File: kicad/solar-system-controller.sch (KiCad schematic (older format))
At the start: 18 parts, among them J1 Raspberry_Pi_2_3, J2 Line_In, U1 MCP3008, U2 500 Gain, U3 1000 Gain

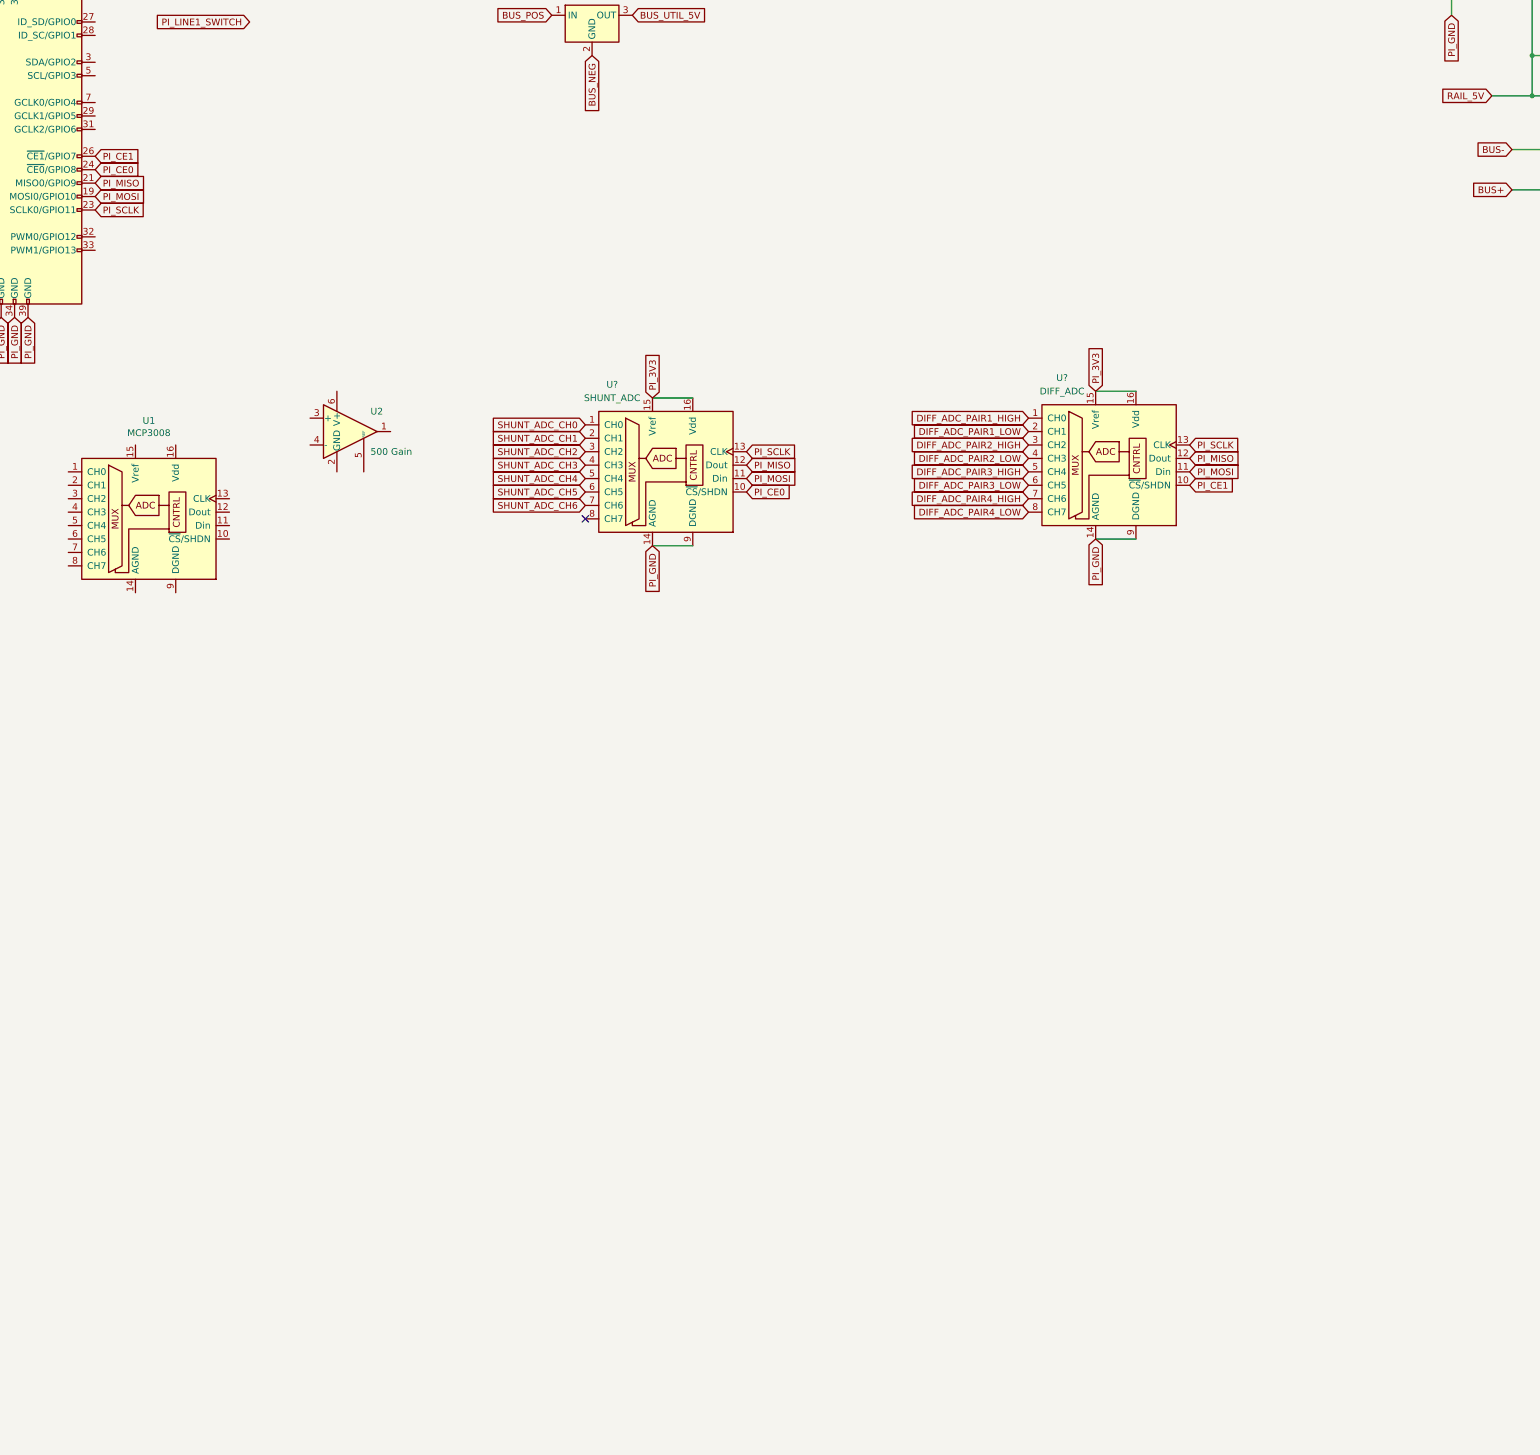
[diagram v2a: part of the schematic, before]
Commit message: Added a mux for the ADCs.
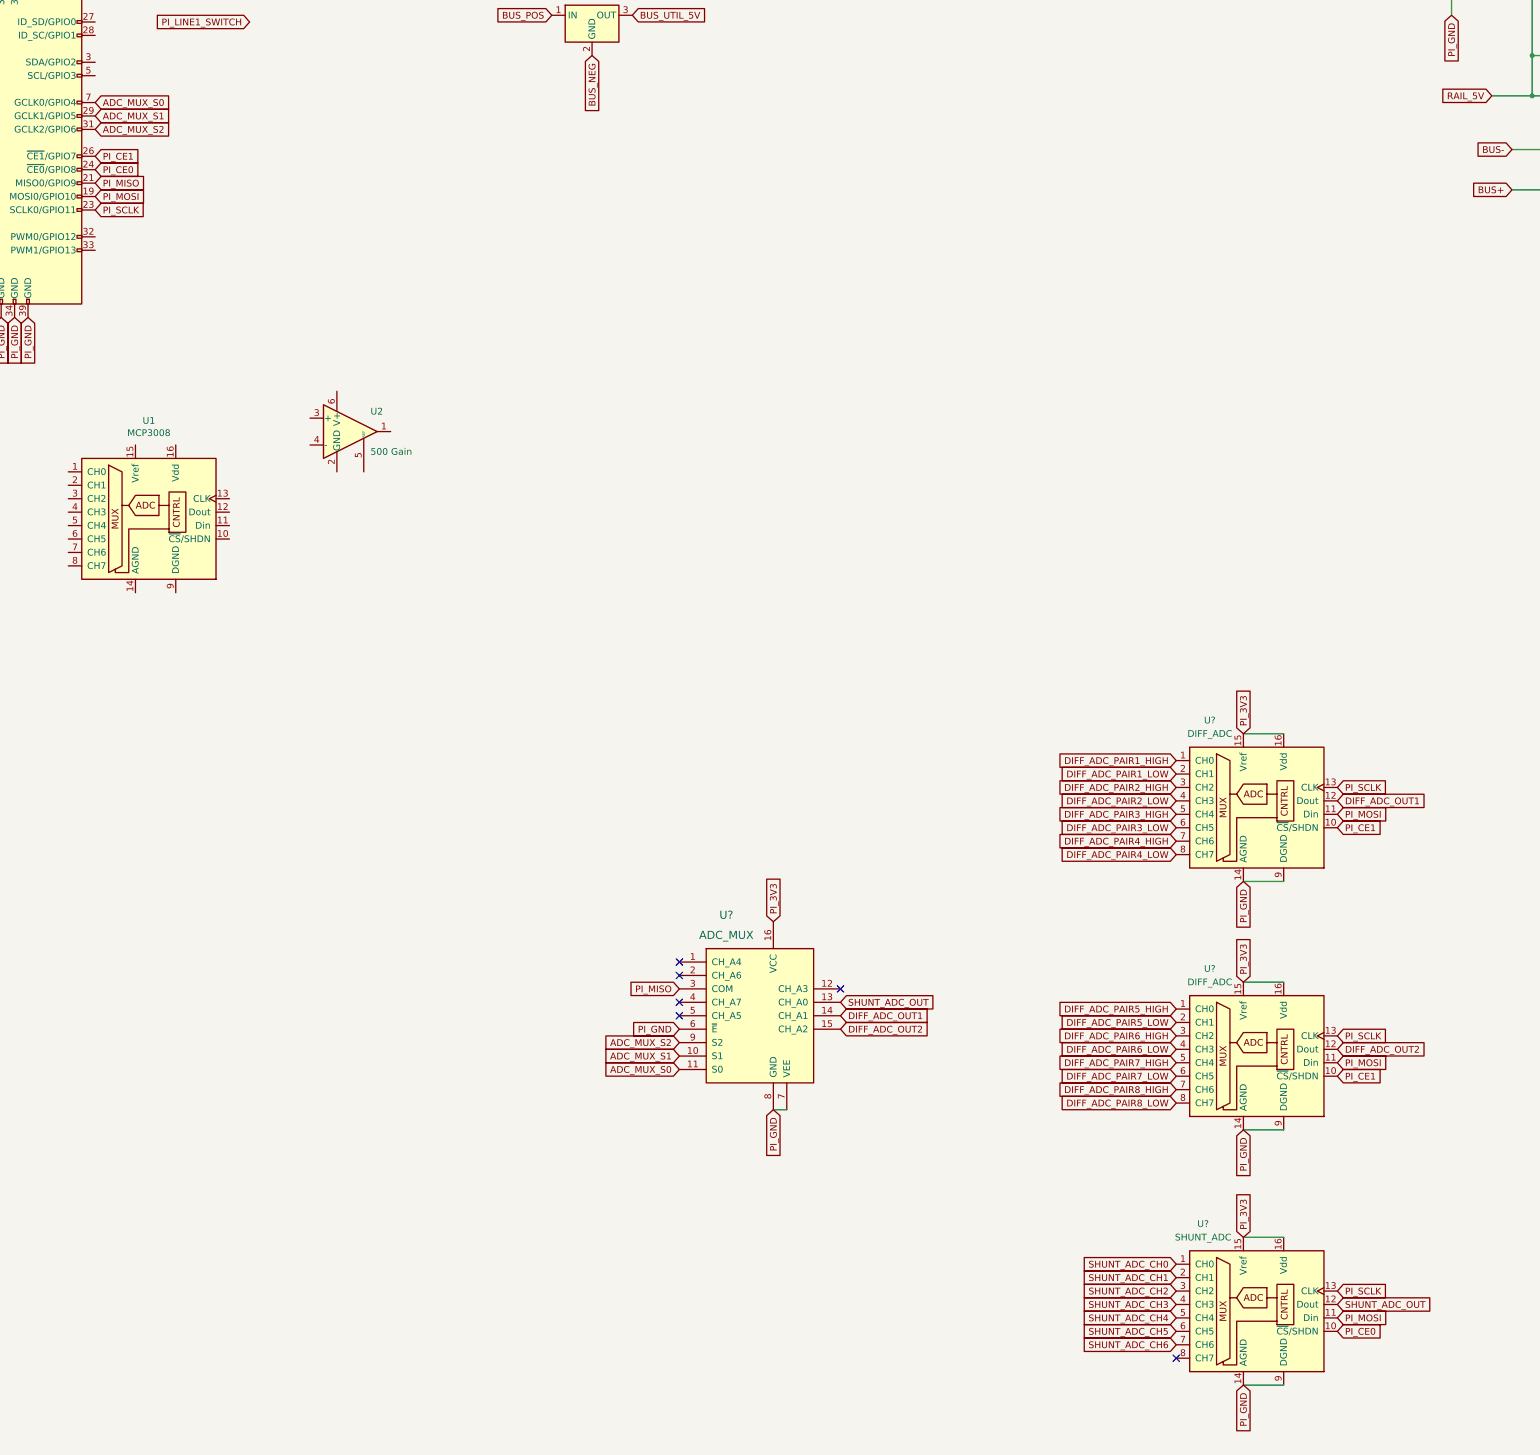
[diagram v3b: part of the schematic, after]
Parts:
- added U?: DIFF_ADC, Package_DIP:DIP-16_W7.62mm, symbol Analog_ADC:MCP3008
- added U?: ADC_MUX, digikey-footprints:DIP-16_W7.62mm, symbol dk_Interface-Analog-Switches-Multiplexers-Demultiplexers:CD74HC4051E
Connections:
- net DIFF_ADC_PAIR1_HIGH: now also U?.1 (CH0); no longer U?.1 (CH0)
- net DIFF_ADC_PAIR1_LOW: now also U?.2 (CH1); no longer U?.2 (CH1)
- net DIFF_ADC_PAIR2_HIGH: now also U?.3 (CH2); no longer U?.3 (CH2)
- net DIFF_ADC_PAIR2_LOW: now also U?.4 (CH3); no longer U?.4 (CH3)
- net DIFF_ADC_PAIR3_HIGH: now also U?.5 (CH4); no longer U?.5 (CH4)
- net DIFF_ADC_PAIR3_LOW: now also U?.6 (CH5); no longer U?.6 (CH5)
- net DIFF_ADC_PAIR4_HIGH: now also U?.7 (CH6); no longer U?.7 (CH6)
- net DIFF_ADC_PAIR4_LOW: now also U?.8 (CH7); no longer U?.8 (CH7)
- net PI_3V3: now also U?.15 (Vref), U?.16 (VCC), U?.16 (Vdd)
- net PI_CE1: now also U?.10 (~CS~/SHDN)
- net PI_GND: now also U?.14 (AGND), U?.6 (~E), U?.7 (VEE), U?.8 (GND), U?.9 (DGND)
- net PI_MISO: now also U?.3 (COM); no longer U?.12 (Dout), U?.12 (Dout)
- net PI_MOSI: now also U?.11 (Din)
- net PI_SCLK: now also U?.13 (CLK)
- net ADC_MUX_S1: now reaches J1.29 (GCLK1/GPIO5)
- net ADC_MUX_S1: now also U?.10 (S1)
- net ADC_MUX_S2: now reaches J1.31 (GCLK2/GPIO6)
- net ADC_MUX_S2: now also U?.9 (S2)
- net ADC_MUX_S0: now reaches J1.7 (GCLK0/GPIO4)
- net ADC_MUX_S0: now also U?.11 (S0)
- new net DIFF_ADC_OUT1: U?.12 (Dout), U?.14 (CH_A1)
- new net DIFF_ADC_OUT2: U?.12 (Dout), U?.15 (CH_A2)
- new net DIFF_ADC_PAIR5_HIGH: U?.1 (CH0)
- new net DIFF_ADC_PAIR5_LOW: U?.2 (CH1)
- new net DIFF_ADC_PAIR6_HIGH: U?.3 (CH2)
- new net DIFF_ADC_PAIR6_LOW: U?.4 (CH3)
- new net DIFF_ADC_PAIR7_HIGH: U?.5 (CH4)
- new net DIFF_ADC_PAIR7_LOW: U?.6 (CH5)
- new net DIFF_ADC_PAIR8_HIGH: U?.7 (CH6)
- new net DIFF_ADC_PAIR8_LOW: U?.8 (CH7)
- new net SHUNT_ADC_OUT: U?.12 (Dout), U?.13 (CH_A0)
- no-connect marks 3 -> 8
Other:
- moved on the sheet: U?
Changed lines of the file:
@@
 L Analog_ADC:MCP3008 U?
 U 1 1 60FB68B4
-P 8150 5450
-F 0 "U?" H 7750 6050 50  0000 C CNN
-F 1 "SHUNT_ADC" H 7750 5950 50  0000 C CNN
-F 2 "Package_DIP:DIP-16_W7.62mm" H 8250 5550 50  0001 C CNN
-F 3 "http://ww1.microchip.com/downloads/en/DeviceDoc/21295d.pdf" H 8250 5550 50  0001 C CNN
-F 4 "https://www.digikey.com/en/products/detail/microchip-technology/MCP3008-I-P/319422" H 8150 5450 50  0001 C CNN "Part"
-	1    8150 5450
-	1    0    0    -1
-$EndComp
-Text GLabel 8050 6050 3    50   Input ~ 0
-PI_GND
-Wire Wire Line
-	8050 6050 8350 6050
-Text GLabel 8050 4950 1    50   Input ~ 0
+P 12550 11700
+F 0 "U?" H 12150 12300 50  0000 C CNN
+F 1 "SHUNT_ADC" H 12150 12200 50  0000 C CNN
+F 2 "Package_DIP:DIP-16_W7.62mm" H 12650 11800 50  0001 C CNN
+F 3 "http://ww1.microchip.com/downloads/en/DeviceDoc/21295d.pdf" H 12650 11800 50  0001 C CNN
+F 4 "https://www.digikey.com/en/products/detail/microchip-technology/MCP3008-I-P/319422" H 12550 11700 50  0001 C CNN "Part"
+	1    12550 11700
+	1    0    0    -1
+$EndComp
+Text GLabel 12450 12300 3    50   Input ~ 0
+PI_GND
+Wire Wire Line
+	12450 12300 12750 12300
+Text GLabel 12450 11200 1    50   Input ~ 0
 PI_3V3
 Wire Wire Line
-	8050 4950 8350 4950
-Text GLabel 7550 5150 0    50   Input ~ 0
+	12450 11200 12750 11200
+Text GLabel 11950 11400 0    50   Input ~ 0
 SHUNT_ADC_CH0
-Text GLabel 7550 5250 0    50   Input ~ 0
+Text GLabel 11950 11500 0    50   Input ~ 0
 SHUNT_ADC_CH1
-Text GLabel 7550 5350 0    50   Input ~ 0
+Text GLabel 11950 11600 0    50   Input ~ 0
 SHUNT_ADC_CH2
-Text GLabel 7550 5450 0    50   Input ~ 0
+Text GLabel 11950 11700 0    50   Input ~ 0
 SHUNT_ADC_CH3
-Text GLabel 7550 5550 0    50   Input ~ 0
+Text GLabel 11950 11800 0    50   Input ~ 0
 SHUNT_ADC_CH4
-Text GLabel 7550 5650 0    50   Input ~ 0
+Text GLabel 11950 11900 0    50   Input ~ 0
 SHUNT_ADC_CH5
-Text GLabel 7550 5750 0    50   Input ~ 0
+Text GLabel 11950 12000 0    50   Input ~ 0
 SHUNT_ADC_CH6
 Text GLabel 15800 4250 3    50   Input ~ 0
@@
 L Analog_ADC:MCP3008 U?
 U 1 1 60FDB10D
-P 11450 5400
-F 0 "U?" H 11100 6000 50  0000 C CNN
-F 1 "DIFF_ADC" H 11100 5900 50  0000 C CNN
-F 2 "Package_DIP:DIP-16_W7.62mm" H 11550 5500 50  0001 C CNN
-F 3 "http://ww1.microchip.com/downloads/en/DeviceDoc/21295d.pdf" H 11550 5500 50  0001 C CNN
-F 4 "https://www.digikey.com/en/products/detail/microchip-technology/MCP3008-I-P/319422" H 11450 5400 50  0001 C CNN "Part"
-	1    11450 5400
-	1    0    0    -1
-$EndComp
-Text GLabel 11350 4900 1    50   Input ~ 0
+P 12550 9800
+F 0 "U?" H 12200 10400 50  0000 C CNN
+F 1 "DIFF_ADC" H 12200 10300 50  0000 C CNN
+F 2 "Package_DIP:DIP-16_W7.62mm" H 12650 9900 50  0001 C CNN
+F 3 "http://ww1.microchip.com/downloads/en/DeviceDoc/21295d.pdf" H 12650 9900 50  0001 C CNN
+F 4 "https://www.digikey.com/en/products/detail/microchip-technology/MCP3008-I-P/319422" H 12550 9800 50  0001 C CNN "Part"
+	1    12550 9800
+	1    0    0    -1
+$EndComp
+Text GLabel 12450 9300 1    50   Input ~ 0
 PI_3V3
 Wire Wire Line
-	11650 4900 11350 4900
-Wire Wire Line
-	11650 6000 11350 6000
-Text GLabel 11350 6000 3    50   Input ~ 0
-PI_GND
-Text GLabel 10850 5100 0    50   Input ~ 0
-DIFF_ADC_PAIR1_HIGH
-Text GLabel 10850 5200 0    50   Input ~ 0
-DIFF_ADC_PAIR1_LOW
-Text GLabel 10850 5300 0    50   Input ~ 0
-DIFF_ADC_PAIR2_HIGH
-Text GLabel 10850 5400 0    50   Input ~ 0
-DIFF_ADC_PAIR2_LOW
-Text GLabel 10850 5500 0    50   Input ~ 0
-DIFF_ADC_PAIR3_HIGH
-Text GLabel 10850 5600 0    50   Input ~ 0
-DIFF_ADC_PAIR3_LOW
-Text GLabel 10850 5700 0    50   Input ~ 0
-DIFF_ADC_PAIR4_HIGH
-Text GLabel 10850 5800 0    50   Input ~ 0
-DIFF_ADC_PAIR4_LOW
+	12750 9300 12450 9300
+Wire Wire Line
+	12750 10400 12450 10400
+Text GLabel 12450 10400 3    50   Input ~ 0
+PI_GND
+Text GLabel 11950 9500 0    50   Input ~ 0
+DIFF_ADC_PAIR5_HIGH
+Text GLabel 11950 9600 0    50   Input ~ 0
+DIFF_ADC_PAIR5_LOW
+Text GLabel 11950 9700 0    50   Input ~ 0
+DIFF_ADC_PAIR6_HIGH
+Text GLabel 11950 9800 0    50   Input ~ 0
+DIFF_ADC_PAIR6_LOW
+Text GLabel 11950 9900 0    50   Input ~ 0
+DIFF_ADC_PAIR7_HIGH
+Text GLabel 11950 10000 0    50   Input ~ 0
+DIFF_ADC_PAIR7_LOW
+Text GLabel 11950 10100 0    50   Input ~ 0
+DIFF_ADC_PAIR8_HIGH
+Text GLabel 11950 10200 0    50   Input ~ 0
+DIFF_ADC_PAIR8_LOW
 Text GLabel 16550 3100 1    50   Input ~ 0
 DIFF_ADC_PAIR1_LOW
@@
 Text GLabel 3900 3550 2    50   Input ~ 0
 PI_SCLK
-Text GLabel 8750 5350 2    50   Input ~ 0
+Text GLabel 13150 11600 2    50   Input ~ 0
 PI_SCLK
 Text GLabel 3900 3350 2    50   Input ~ 0
 PI_MISO
-Text GLabel 8750 5450 2    50   Input ~ 0
-PI_MISO
+Text GLabel 13150 11700 2    50   Input ~ 0
+SHUNT_ADC_OUT
 Text GLabel 3900 3450 2    50   Input ~ 0
 PI_MOSI
-Text GLabel 8750 5550 2    50   Input ~ 0
+Text GLabel 13150 11800 2    50   Input ~ 0
 PI_MOSI
 Text GLabel 3900 3250 2    50   Input ~ 0
@@
 Text GLabel 3900 3150 2    50   Input ~ 0
 PI_CE1
-Text GLabel 8750 5650 2    50   Input ~ 0
+Text GLabel 13150 11900 2    50   Input ~ 0
 PI_CE0
-NoConn ~ 7550 5850
-Text GLabel 12050 5300 2    50   Input ~ 0
+NoConn ~ 11950 12100
+Text GLabel 13150 9700 2    50   Input ~ 0
 PI_SCLK
-Text GLabel 12050 5400 2    50   Input ~ 0
-PI_MISO
-Text GLabel 12050 5500 2    50   Input ~ 0
+Text GLabel 13150 9800 2    50   Input ~ 0
+DIFF_ADC_OUT2
+Text GLabel 13150 9900 2    50   Input ~ 0
 PI_MOSI
-Text GLabel 12050 5600 2    50   Input ~ 0
+Text GLabel 13150 10000 2    50   Input ~ 0
 PI_CE1
 Text GLabel 2300 3750 0    50   Input ~ 0
 PI_CE3
+$Comp
+L Analog_ADC:MCP3008 U?
+U 1 1 61057BC9
+P 12550 7950
+F 0 "U?" H 12200 8550 50  0000 C CNN
+F 1 "DIFF_ADC" H 12200 8450 50  0000 C CNN
+F 2 "Package_DIP:DIP-16_W7.62mm" H 12650 8050 50  0001 C CNN
+F 3 "http://ww1.microchip.com/downloads/en/DeviceDoc/21295d.pdf" H 12650 8050 50  0001 C CNN
+F 4 "https://www.digikey.com/en/products/detail/microchip-technology/MCP3008-I-P/319422" H 12550 7950 50  0001 C CNN "Part"
+	1    12550 7950
+	1    0    0    -1
+$EndComp
+Text GLabel 12450 7450 1    50   Input ~ 0
+PI_3V3
+Wire Wire Line
+	12750 7450 12450 7450
+Wire Wire Line
+	12750 8550 12450 8550
+Text GLabel 12450 8550 3    50   Input ~ 0
+PI_GND
+Text GLabel 11950 7650 0    50   Input ~ 0
+DIFF_ADC_PAIR1_HIGH
+Text GLabel 11950 7750 0    50   Input ~ 0
+DIFF_ADC_PAIR1_LOW
+Text GLabel 11950 7850 0    50   Input ~ 0
+DIFF_ADC_PAIR2_HIGH
+Text GLabel 11950 7950 0    50   Input ~ 0
+DIFF_ADC_PAIR2_LOW
+Text GLabel 11950 8050 0    50   Input ~ 0
+DIFF_ADC_PAIR3_HIGH
+Text GLabel 11950 8150 0    50   Input ~ 0
+DIFF_ADC_PAIR3_LOW
+Text GLabel 11950 8250 0    50   Input ~ 0
+DIFF_ADC_PAIR4_HIGH
+Text GLabel 11950 8350 0    50   Input ~ 0
+DIFF_ADC_PAIR4_LOW
+Text GLabel 13150 7850 2    50   Input ~ 0
+PI_SCLK
+Text GLabel 13150 7950 2    50   Input ~ 0
+DIFF_ADC_OUT1
+Text GLabel 13150 8050 2    50   Input ~ 0
+PI_MOSI
+Text GLabel 13150 8150 2    50   Input ~ 0
+PI_CE1
+$Comp
+L dk_Interface-Analog-Switches-Multiplexers-Demultiplexers:CD74HC4051E U?
+U 1 1 61078403
+P 8850 9550
+F 0 "U?" H 8600 10300 60  0000 C CNN
+F 1 "ADC_MUX" H 8600 10150 60  0000 C CNN
+F 2 "digikey-footprints:DIP-16_W7.62mm" H 9050 9750 60  0001 L CNN
+F 3 "http://www.ti.com/general/docs/suppproductinfo.tsp?distId=10&gotoUrl=http%3A%2F%2Fwww.ti.com%2Flit%2Fgpn%2Fcd74hc4051" H 9050 9850 60  0001 L CNN
+F 4 "296-12810-5-ND" H 9050 9950 60  0001 L CNN "Digi-Key_PN"
+F 5 "CD74HC4051E" H 9050 10050 60  0001 L CNN "MPN"
+F 6 "Integrated Circuits (ICs)" H 9050 10150 60  0001 L CNN "Category"
+F 7 "Interface - Analog Switches, Multiplexers, Demultiplexers" H 9050 10250 60  0001 L CNN "Family"
+F 8 "http://www.ti.com/general/docs/suppproductinfo.tsp?distId=10&gotoUrl=http%3A%2F%2Fwww.ti.com%2Flit%2Fgpn%2Fcd74hc4051" H 9050 10350 60  0001 L CNN "DK_Datasheet_Link"
+F 9 "/product-detail/en/texas-instruments/CD74HC4051E/296-12810-5-ND/475938" H 9050 10450 60  0001 L CNN "DK_Detail_Page"
+F 10 "IC MUX/DEMUX 8X1 16DIP" H 9050 10550 60  0001 L CNN "Description"
+F 11 "Texas Instruments" H 9050 10650 60  0001 L CNN "Manufacturer"
+F 12 "Active" H 9050 10750 60  0001 L CNN "Status"
+F 13 "http://digikey.com/en/products/detail/texas-instruments/CD74HC4051E/475938?s=N4IgTCBcDaIMIBEDsAWAEnFAGArARgFEQBdAXyA" H 8850 9550 50  0001 C CNN "Part"
+	1    8850 9550
+	1    0    0    -1
+$EndComp
+Text GLabel 8950 8850 1    50   Input ~ 0
+PI_3V3
+Text GLabel 8950 10250 3    50   Input ~ 0
+PI_GND
+Wire Wire Line
+	8950 10250 9050 10250
+NoConn ~ 9450 9350
+NoConn ~ 8250 9150
+NoConn ~ 8250 9250
+NoConn ~ 8250 9450
+NoConn ~ 8250 9550
+Text GLabel 8250 9350 0    50   Input ~ 0
+PI_MISO
+Text GLabel 9450 9550 2    50   Input ~ 0
+DIFF_ADC_OUT1
+Text GLabel 9450 9650 2    50   Input ~ 0
+DIFF_ADC_OUT2
+Text GLabel 9450 9450 2    50   Input ~ 0
+SHUNT_ADC_OUT
+Text GLabel 8250 9650 0    50   Input ~ 0
+PI_GND
+Text GLabel 8250 9850 0    50   Input ~ 0
+ADC_MUX_S1
+Text GLabel 8250 9950 0    50   Input ~ 0
+ADC_MUX_S0
+Text GLabel 8250 9750 0    50   Input ~ 0
+ADC_MUX_S2
+Text GLabel 3900 2950 2    50   Input ~ 0
+ADC_MUX_S2
+Text GLabel 3900 2850 2    50   Input ~ 0
+ADC_MUX_S1
+Text GLabel 3900 2750 2    50   Input ~ 0
+ADC_MUX_S0
 $EndSCHEMATC
